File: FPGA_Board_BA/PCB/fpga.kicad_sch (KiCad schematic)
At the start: 5 parts, among them J9 Box_Header_26pin, U2 Zynq7020

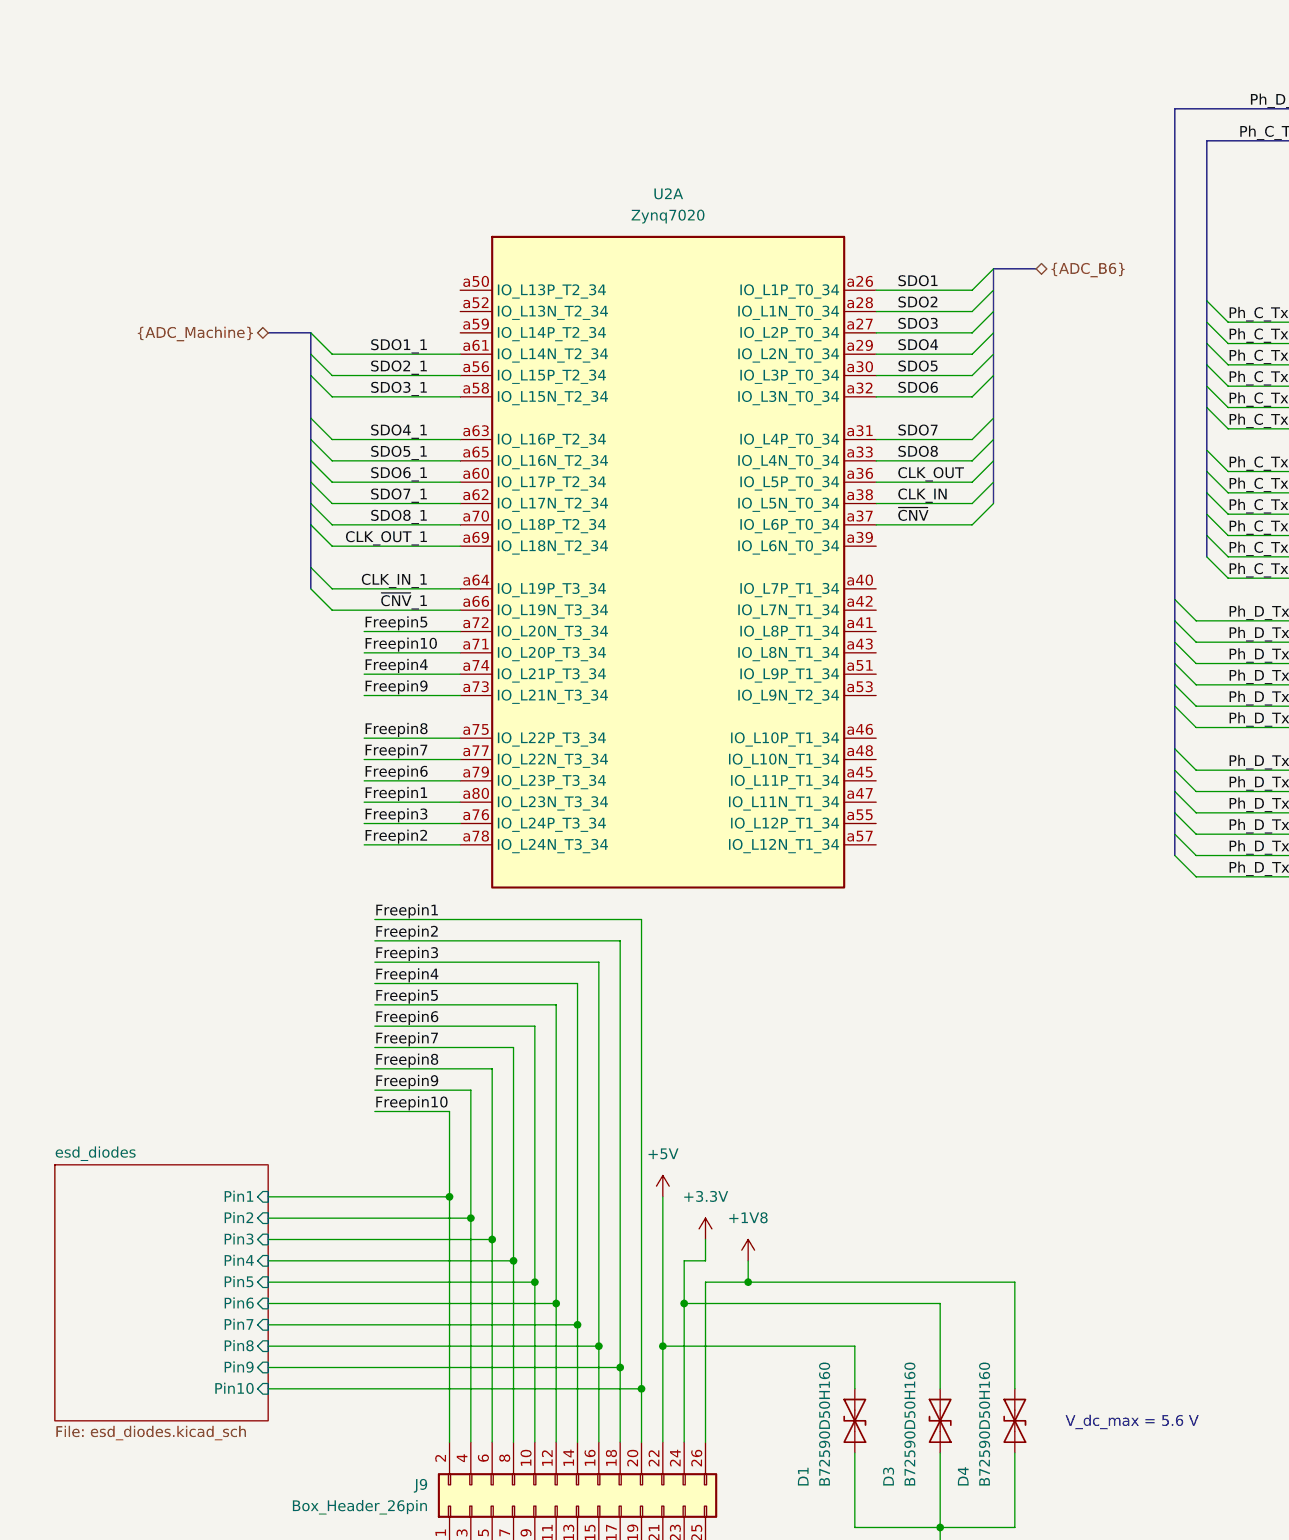
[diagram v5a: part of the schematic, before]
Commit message: optimised pinout in schematic + added level shifter for CLKOUT + got forward with layout
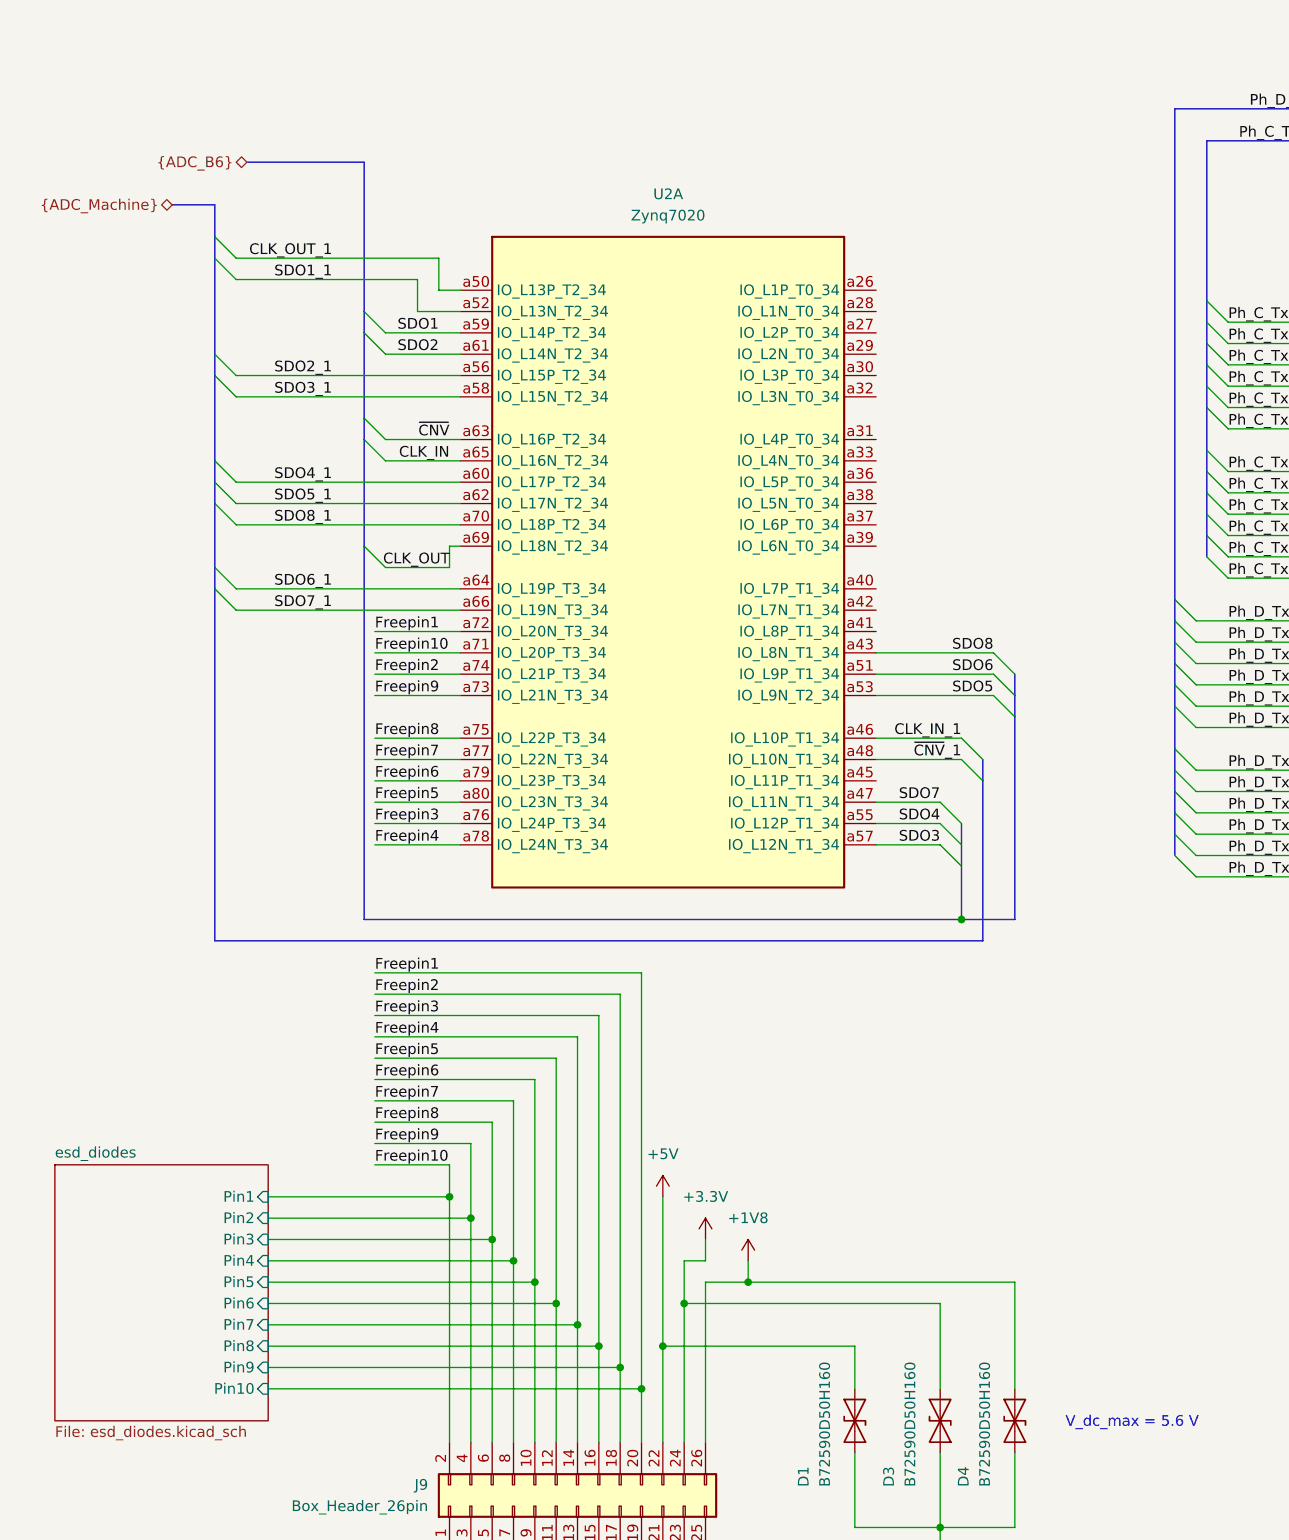
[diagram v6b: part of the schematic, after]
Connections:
- net CLK_IN: now also U2.a65 (IO_L16N_T2_34); no longer U2.a38 (IO_L5N_T0_34)
- net CLK_IN_1: now also U2.a46 (IO_L10P_T1_34); no longer U2.a64 (IO_L19P_T3_34)
- net CLK_OUT: now also U2.a69 (IO_L18N_T2_34); no longer U2.a36 (IO_L5P_T0_34)
- net CLK_OUT_1: now also U2.a50 (IO_L13P_T2_34); no longer U2.a69 (IO_L18N_T2_34)
- net Freepin1: now also U2.a72 (IO_L20N_T3_34); no longer U2.a80 (IO_L23N_T3_34)
- net Freepin2: now also U2.a74 (IO_L21P_T3_34); no longer U2.a78 (IO_L24N_T3_34)
- net Freepin4: now also U2.a78 (IO_L24N_T3_34); no longer U2.a74 (IO_L21P_T3_34)
- net Freepin5: now also U2.a80 (IO_L23N_T3_34); no longer U2.a72 (IO_L20N_T3_34)
- net SDO1: now also U2.a59 (IO_L14P_T2_34); no longer U2.a26 (IO_L1P_T0_34)
- net SDO1_1: now also U2.a52 (IO_L13N_T2_34); no longer U2.a61 (IO_L14N_T2_34)
- net SDO2: now also U2.a61 (IO_L14N_T2_34); no longer U2.a28 (IO_L1N_T0_34)
- net SDO3: now also U2.a57 (IO_L12N_T1_34); no longer U2.a27 (IO_L2P_T0_34)
- net SDO4: now also U2.a55 (IO_L12P_T1_34); no longer U2.a29 (IO_L2N_T0_34)
- net SDO4_1: now also U2.a60 (IO_L17P_T2_34); no longer U2.a63 (IO_L16P_T2_34)
- net SDO5: now also U2.a53 (IO_L9N_T2_34); no longer U2.a30 (IO_L3P_T0_34)
- net SDO5_1: now also U2.a62 (IO_L17N_T2_34); no longer U2.a65 (IO_L16N_T2_34)
- net SDO6: now also U2.a51 (IO_L9P_T1_34); no longer U2.a32 (IO_L3N_T0_34)
- net SDO6_1: now also U2.a64 (IO_L19P_T3_34); no longer U2.a60 (IO_L17P_T2_34)
- net SDO7: now also U2.a47 (IO_L11N_T1_34); no longer U2.a31 (IO_L4P_T0_34)
- net SDO7_1: now also U2.a66 (IO_L19N_T3_34); no longer U2.a62 (IO_L17N_T2_34)
- net SDO8: now also U2.a43 (IO_L8N_T1_34); no longer U2.a33 (IO_L4N_T0_34)
- net ~{CNV}: now also U2.a63 (IO_L16P_T2_34); no longer U2.a37 (IO_L6P_T0_34)
- net ~{CNV}_1: now also U2.a48 (IO_L10N_T1_34); no longer U2.a66 (IO_L19N_T3_34)

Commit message: fixed wire bus in schematic + routing almost ready, only routing of power is left
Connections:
- net B6_En: now also U2.a27 (IO_L2P_T0_34); no longer U2.a16 (IO_L14P_T2_13)
- net Button1: now also U2.a7 (IO_L11P_T1_13)
- net Button2: now also U2.a9 (IO_L11N_T1_13)
- net ENC_A: now also U2.a19 (IO_L13N_T2_13)
- net ENC_B: now also U2.a21 (IO_L15P_T2_13)
- net ENC_I: now also U2.a23 (IO_L15N_T2_13)
- net En_Ph1: now also U2.a26 (IO_L1P_T0_34)
- net En_Ph2: now also U2.a30 (IO_L3P_T0_34)
- net En_Ph3: now also U2.a36 (IO_L5P_T0_34)
- net En_Ph4: now also U2.a40 (IO_L7P_T1_34)
- net Err_Ph1: now also U2.a22 (IO_L21N_T3_13)
- net Err_Ph2: now also U2.a20 (IO_L21P_T3_13)
- net Err_Ph3: now also U2.a18 (IO_L14N_T2_13)
- net Err_Ph4: now also U2.a16 (IO_L14P_T2_13)
- net LED1: now also U2.a11 (IO_L12P_T1_13)
- net LED2: now also U2.a13 (IO_L12N_T1_13)
- net LED3: now also U2.a17 (IO_L13P_T2_13)
- net OT: now also U2.a29 (IO_L2N_T0_34); no longer U2.a18 (IO_L14N_T2_13)
- net PWM_AH: now also U2.a45 (IO_L11P_T1_34); no longer U2.a7 (IO_L11P_T1_13)
- net PWM_AL: now also U2.a41 (IO_L8P_T1_34); no longer U2.a9 (IO_L11N_T1_13)
- net PWM_BH: now also U2.a39 (IO_L6N_T0_34); no longer U2.a11 (IO_L12P_T1_13)
- net PWM_BL: now also U2.a37 (IO_L6P_T0_34); no longer U2.a13 (IO_L12N_T1_13)
- net PWM_CH: now also U2.a33 (IO_L4N_T0_34); no longer U2.a17 (IO_L13P_T2_13)
- net PWM_CL: now also U2.a31 (IO_L4P_T0_34); no longer U2.a19 (IO_L13N_T2_13)
- net Rx_Ph1: now also U2.a28 (IO_L1N_T0_34)
- net Rx_Ph2: now also U2.a32 (IO_L3N_T0_34)
- net Rx_Ph3: now also U2.a38 (IO_L5N_T0_34)
- net Rx_Ph4: now also U2.a42 (IO_L7N_T1_34)
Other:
- moved on the sheet: U2C, U2D
